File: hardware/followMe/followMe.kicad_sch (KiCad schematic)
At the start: 26 parts, among them J1 FTDI, J2 I2C, J3 Analog, J4 Vi+, J5 Vi-, J6 Analog, J7 Digital, J8 Vo-, J9 Vo+, Q1 MMBT2222A, SW1 SW_Push_LED, SW2 SW_Push_LED, SW3 SW_Push_LED, SW4 SW_Push_LED

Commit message: version 1.00
First Versiyon
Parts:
- renumbered R1 to R101, R2 to R102, R3 to R103, R4 to R104, R5 to R105, R6 to R106, R7 to R107, R8 to R108, R9 to R109, R10 to R110
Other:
- added sheet schineder button led circuit (untitled.kicad_sch)
- moved on the sheet: BZ1, Q1, R101, R102

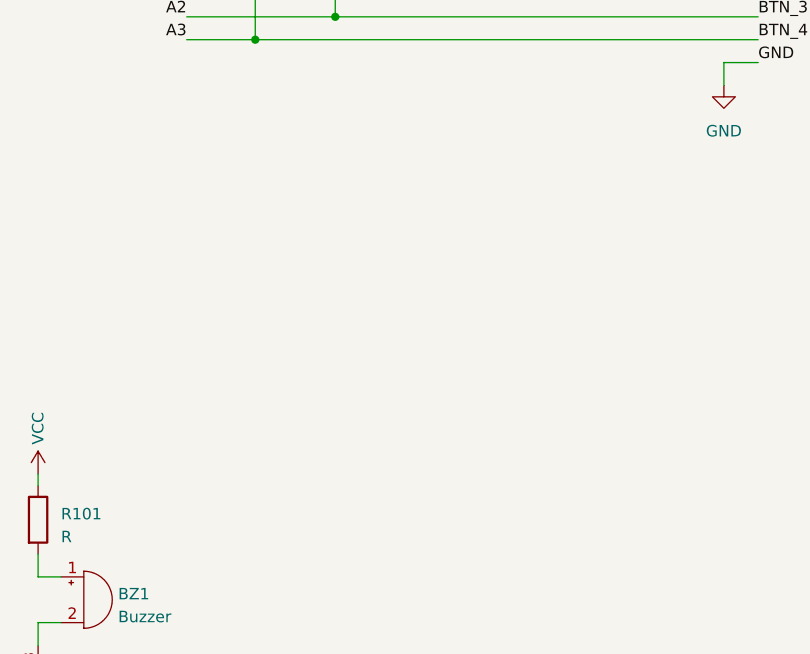
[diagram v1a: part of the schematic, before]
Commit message: v1.01
Grafik LCD Ekran Eklendi
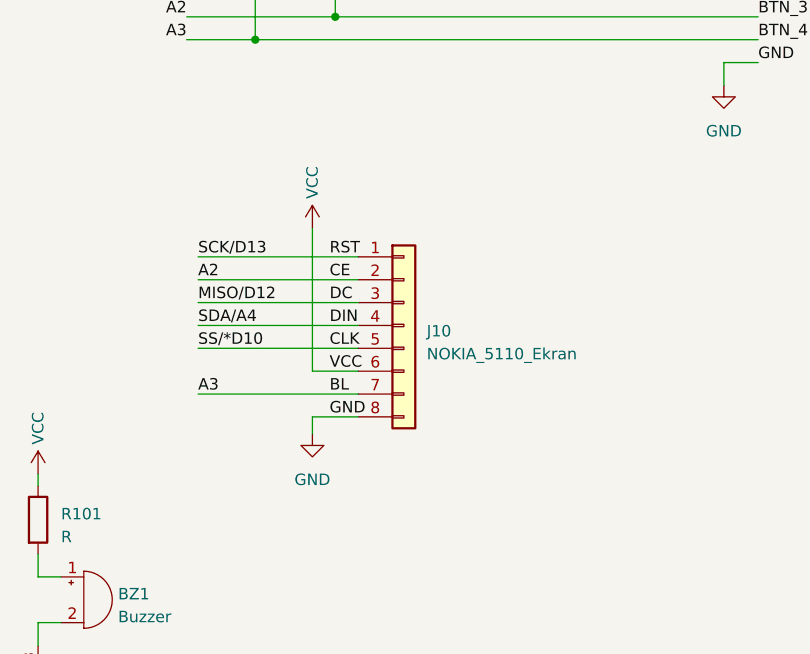
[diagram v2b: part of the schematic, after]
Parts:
- added J10: NOKIA_5110_Ekran, symbol Connector_Generic:Conn_01x08
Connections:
- net A2: now also J10.2 (Pin_2)
- net A3: now also J10.7 (Pin_7)
- net GND: now also J10.8 (Pin_8)
- net VCC: now also J10.6 (Pin_6)
- net MISO/D12 renamed DC
- net DC: now also J10.3 (Pin_3)
- net SCK/D13 renamed RST
- net RST: now also J10.1 (Pin_1)
- net SDA/A4 renamed DIN
- net DIN: now also J10.4 (Pin_4)
- net SS/*D10 renamed CLK
- net CLK: now also J10.5 (Pin_5)
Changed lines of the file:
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@@
     (stroke (width 0) (type solid))
+  )
+  (wire (pts (xy 132.08 106.68) (xy 137.16 106.68))
+    (stroke (width 0) (type default))
   )
   (wire (pts (xy 118.11 69.85) (xy 125.73 69.85))
@@
     (stroke (width 0) (type default))
   )
+  (wire (pts (xy 132.08 111.76) (xy 132.08 113.665))
+    (stroke (width 0) (type default))
+  )
   (wire (pts (xy 38.1 26.67) (xy 38.1 29.21))
     (stroke (width 0) (type solid))
@@
     (stroke (width 0) (type solid))
   )
+  (wire (pts (xy 119.38 109.22) (xy 137.16 109.22))
+    (stroke (width 0) (type default))
+  )
+  (wire (pts (xy 119.38 99.06) (xy 137.16 99.06))
+    (stroke (width 0) (type default))
+  )
   (wire (pts (xy 177.8 72.39) (xy 181.61 72.39))
     (stroke (width 0) (type default))
@@
     (stroke (width 0) (type default))
   )
+  (wire (pts (xy 119.38 104.14) (xy 137.16 104.14))
+    (stroke (width 0) (type default))
+  )
   (wire (pts (xy 142.24 64.77) (xy 181.61 64.77))
     (stroke (width 0) (type default))
   )
+  (wire (pts (xy 132.08 111.76) (xy 137.16 111.76))
+    (stroke (width 0) (type default))
+  )
   (wire (pts (xy 55.88 52.07) (xy 60.96 52.07))
     (stroke (width 0) (type solid))
@@
     (stroke (width 0) (type default))
   )
+  (wire (pts (xy 119.38 96.52) (xy 137.16 96.52))
+    (stroke (width 0) (type default))
+  )
   (wire (pts (xy 67.31 125.73) (xy 67.31 128.27))
     (stroke (width 0) (type default))
@@
     (stroke (width 0) (type default))
   )
+  (wire (pts (xy 119.38 101.6) (xy 137.16 101.6))
+    (stroke (width 0) (type default))
+  )
   (wire (pts (xy 101.6 127) (xy 101.6 129.54))
     (stroke (width 0) (type default))
@@
     (stroke (width 0) (type solid))
   )
+  (wire (pts (xy 119.38 93.98) (xy 137.16 93.98))
+    (stroke (width 0) (type default))
+  )
   (wire (pts (xy 125.73 59.69) (xy 125.73 69.85))
     (stroke (width 0) (type default))
@@
     (stroke (width 0) (type default))
   )
+  (wire (pts (xy 132.08 90.805) (xy 132.08 106.68))
+    (stroke (width 0) (type default))
+  )
+  (label "CLK" (at 133.985 104.14 0) (fields_autoplaced)
+    (effects (font (size 1.27 1.27)) (justify left bottom))
+  )
   (label "LED_4" (at 181.61 59.69 0) (fields_autoplaced)
     (effects (font (size 1.27 1.27)) (justify left bottom))
@@
     (effects (font (size 1.27 1.27)) (justify left bottom))
   )
+  (label "A3" (at 119.38 109.22 0) (fields_autoplaced)
+    (effects (font (size 1.27 1.27)) (justify left bottom))
+  )
+  (label "A2" (at 119.38 96.52 0) (fields_autoplaced)
+    (effects (font (size 1.27 1.27)) (justify left bottom))
+  )
   (label "A2" (at 71.12 57.15 180) (fields_autoplaced)
     (effects (font (size 1.27 1.27)) (justify right bottom))
   )
+  (label "VCC" (at 133.985 106.68 0) (fields_autoplaced)
+    (effects (font (size 1.27 1.27)) (justify left bottom))
+  )
   (label "A0" (at 71.12 62.23 180) (fields_autoplaced)
     (effects (font (size 1.27 1.27)) (justify right bottom))
@@
     (effects (font (size 1.27 1.27)) (justify left bottom))
   )
+  (label "MISO{slash}D12" (at 119.38 99.06 0) (fields_autoplaced)
+    (effects (font (size 1.27 1.27)) (justify left bottom))
+  )
+  (label "SDA{slash}A4" (at 119.38 101.6 0) (fields_autoplaced)
+    (effects (font (size 1.27 1.27)) (justify left bottom))
+  )
   (label "SDA{slash}A4" (at 66.04 85.09 180) (fields_autoplaced)
     (effects (font (size 1.27 1.27)) (justify right bottom))
@@
     (effects (font (size 1.27 1.27)) (justify left bottom))
   )
+  (label "BL" (at 133.985 109.22 0) (fields_autoplaced)
+    (effects (font (size 1.27 1.27)) (justify left bottom))
+  )
+  (label "SCK{slash}D13" (at 119.38 93.98 0) (fields_autoplaced)
+    (effects (font (size 1.27 1.27)) (justify left bottom))
+  )
   (label "GND" (at 189.23 72.39 0) (fields_autoplaced)
     (effects (font (size 1.27 1.27)) (justify left bottom))
@@
     (effects (font (size 1.27 1.27)) (justify left bottom))
   )
+  (label "RST" (at 133.985 93.98 0) (fields_autoplaced)
+    (effects (font (size 1.27 1.27)) (justify left bottom))
+  )
   (label "*D5" (at 161.29 59.69 0) (fields_autoplaced)
     (effects (font (size 1.27 1.27)) (justify left bottom))
@@
     (effects (font (size 1.27 1.27)) (justify left bottom))
   )
+  (label "DC" (at 133.985 99.06 0) (fields_autoplaced)
+    (effects (font (size 1.27 1.27)) (justify left bottom))
+  )
+  (label "DIN" (at 133.985 101.6 0) (fields_autoplaced)
+    (effects (font (size 1.27 1.27)) (justify left bottom))
+  )
   (label "RX" (at 45.72 24.13 270) (fields_autoplaced)
     (effects (font (size 1.27 1.27)) (justify right bottom))
   )
+  (label "CE" (at 133.985 96.52 0) (fields_autoplaced)
+    (effects (font (size 1.27 1.27)) (justify left bottom))
+  )
   (label "A0" (at 118.11 62.23 180) (fields_autoplaced)
     (effects (font (size 1.27 1.27)) (justify right bottom))
   )
+  (label "GND" (at 133.985 111.76 0) (fields_autoplaced)
+    (effects (font (size 1.27 1.27)) (justify left bottom))
+  )
   (label "BTN_3" (at 181.61 67.31 0) (fields_autoplaced)
     (effects (font (size 1.27 1.27)) (justify left bottom))
@@
   (label "A3" (at 71.12 54.61 180) (fields_autoplaced)
     (effects (font (size 1.27 1.27)) (justify right bottom))
+  )
+  (label "SS{slash}*D10" (at 119.38 104.14 0) (fields_autoplaced)
+    (effects (font (size 1.27 1.27)) (justify left bottom))
   )
   (label "A2" (at 118.11 67.31 180) (fields_autoplaced)
@@
     )
   )
+  (symbol (lib_id "Connector_Generic:Conn_01x08") (at 142.24 101.6 0) (unit 1)
+    (in_bom yes) (on_board yes) (dnp no) (fields_autoplaced)
+    (property "Reference" "J10" (at 144.78 102.235 0)
+      (effects (font (size 1.27 1.27)) (justify left))
+    )
+    (property "Value" "NOKIA_5110_Ekran" (at 144.78 104.775 0)
+      (effects (font (size 1.27 1.27)) (justify left))
+    )
+    (property "Footprint" "" (at 142.24 101.6 0)
+      (effects (font (size 1.27 1.27)) hide)
+    )
+    (property "Datasheet" "~" (at 142.24 101.6 0)
+      (effects (font (size 1.27 1.27)) hide)
+    )
+    (pin "1")
+    (pin "2")
+    (pin "3")
+    (pin "4")
+    (pin "5")
+    (pin "6")
+    (pin "7")
+    (pin "8")
+    (instances
+      (project "followMe"
+        (path "/e63e39d7-6ac0-4ffd-8aa3-1841a4541b55"
+          (reference "J10") (unit 1)
+        )
+      )
+    )
+  )
   (symbol (lib_id "Device:Buzzer") (at 106.68 132.08 0) (unit 1)
     (in_bom yes) (on_board yes) (dnp no) (fields_autoplaced)
@@
     )
   )
+  (symbol (lib_id "power:VCC") (at 132.08 90.805 0) (unit 1)
+    (in_bom yes) (on_board yes) (dnp no)
+    (property "Reference" "#PWR011" (at 132.08 94.615 0)
+      (effects (font (size 1.27 1.27)) hide)
+    )
+    (property "Value" "VCC" (at 132.08 85.725 90)
+      (effects (font (size 1.27 1.27)))
+    )
+    (property "Footprint" "" (at 132.08 90.805 0)
+      (effects (font (size 1.27 1.27)) hide)
+    )
+    (property "Datasheet" "" (at 132.08 90.805 0)
+      (effects (font (size 1.27 1.27)) hide)
+    )
+    (pin "1")
+    (instances
+      (project "followMe"
+        (path "/e63e39d7-6ac0-4ffd-8aa3-1841a4541b55"
+          (reference "#PWR011") (unit 1)
+        )
+      )
+    )
+  )
   (symbol (lib_id "Device:R") (at 173.99 59.69 90) (unit 1)
     (in_bom yes) (on_board yes) (dnp no)
@@
         )
       )
+    )
+  )
+  (symbol (lib_name "GND_1") (lib_id "power:GND") (at 132.08 113.665 0) (unit 1)
+    (in_bom yes) (on_board yes) (dnp no) (fields_autoplaced)
+    (property "Reference" "#PWR010" (at 132.08 120.015 0)
+      (effects (font (size 1.27 1.27)) hide)
+    )
+    (property "Value" "GND" (at 132.08 118.745 0)
+      (effects (font (size 1.27 1.27)))
+    )
+    (property "Footprint" "" (at 132.08 113.665 0)
+      (effects (font (size 1.27 1.27)) hide)
+    )
+    (property "Datasheet" "" (at 132.08 113.665 0)
+      (effects (font (size 1.27 1.27)) hide)
+    )
+    (pin "1")
+    (instances
+      (project "followMe"
+        (path "/e63e39d7-6ac0-4ffd-8aa3-1841a4541b55"
+          (reference "#PWR010") (unit 1)
+        )
+      )

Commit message: Revert "GLCD ekran eklendi"
This reverts commit 4725419bf9b5e84ee3984d31ef229cf3f0ee9c22.
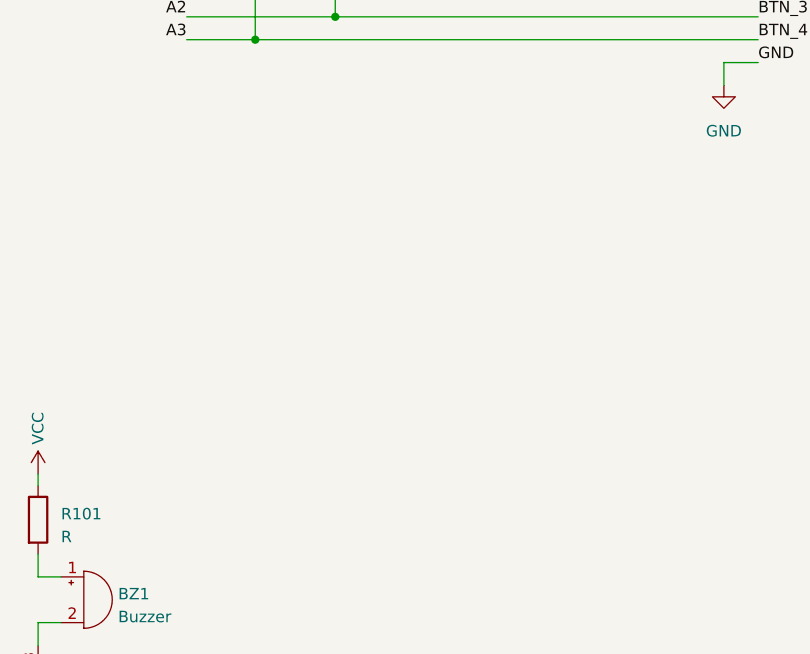
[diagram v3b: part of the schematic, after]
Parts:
- removed J10: NOKIA_5110_Ekran, symbol Connector_Generic:Conn_01x08
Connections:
- net CLK renamed SS/*D10
- net DC renamed MISO/D12
- net DIN renamed SDA/A4
- net RST renamed SCK/D13
